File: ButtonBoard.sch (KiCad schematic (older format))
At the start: 4 parts, among them J1 Conn_01x06_Male

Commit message: rearrange and plot for build
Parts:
- D1: footprint LED_THT:LED_D3.0mm -> LEDs:LED_Rectangular_W3.0mm_H2.0mm
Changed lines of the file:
@@
 F 0 "D1" H 6443 2866 50  0000 C CNN
 F 1 "LED" H 6443 2775 50  0000 C CNN
-F 2 "LED_THT:LED_D3.0mm" H 6450 2650 50  0001 C CNN
+F 2 "LEDs:LED_Rectangular_W3.0mm_H2.0mm" H 6450 2650 50  0001 C CNN
 F 3 "~" H 6450 2650 50  0001 C CNN
 	1    6450 2650

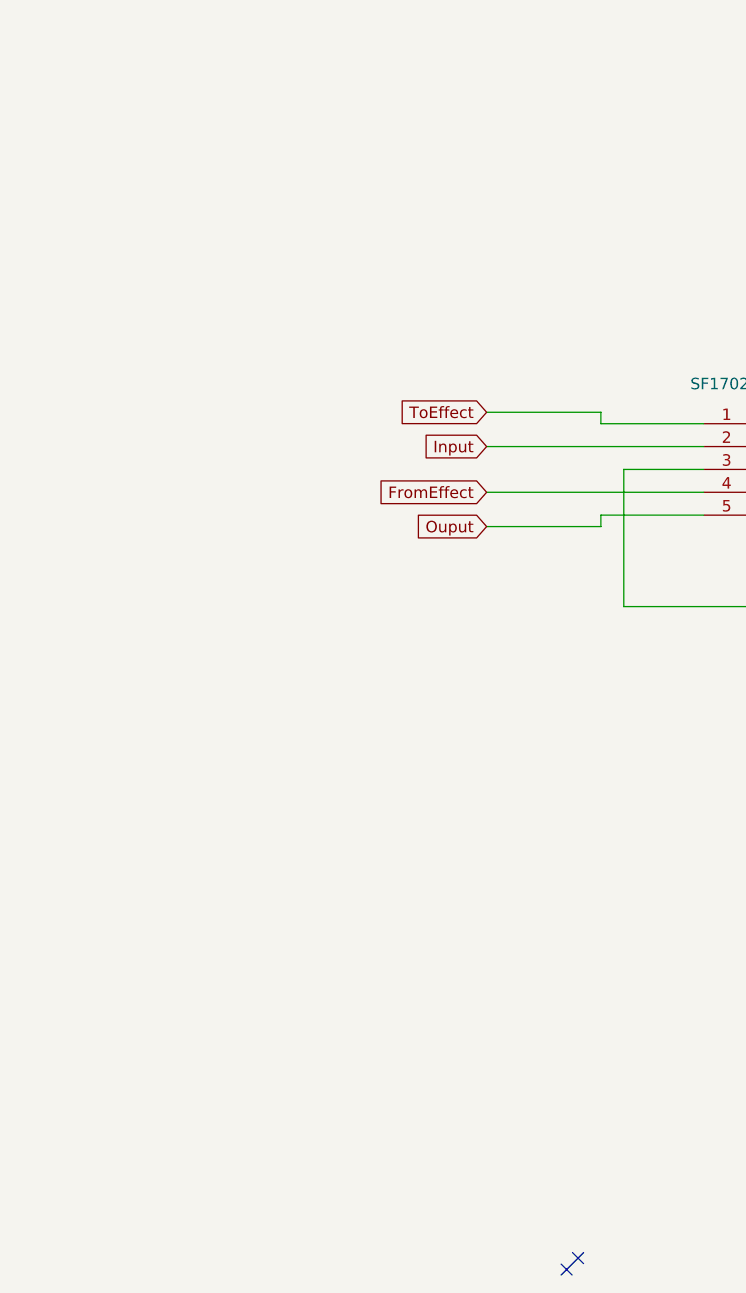
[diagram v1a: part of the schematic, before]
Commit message: Bump to version 1.2 make the holes a little bigger
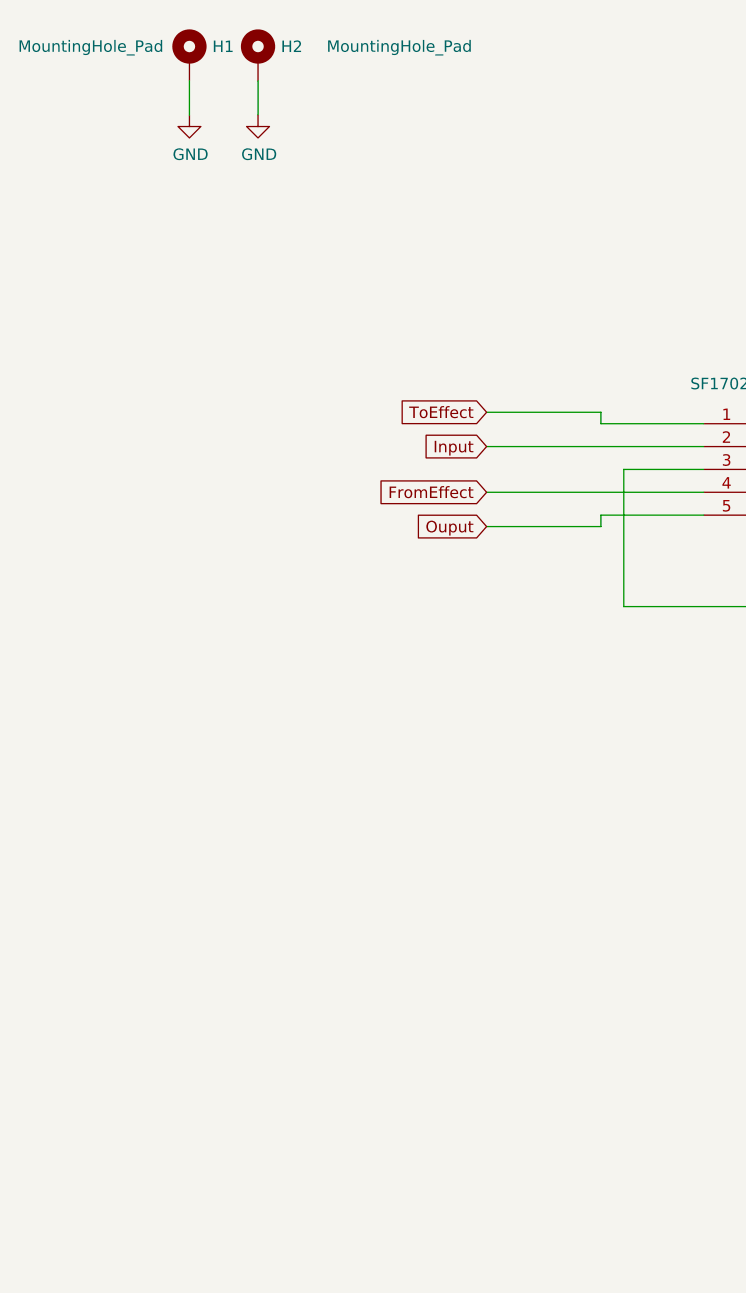
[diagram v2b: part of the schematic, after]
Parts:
- added H1, H2: MountingHole_Pad, Wire_Pads:SolderWirePad_single_1mmDrill, symbol Mechanical:MountingHole_Pad
- S1: footprint SF17020F-0302-21R-L-015:SF17020F030221RL015 -> Footswitch:Footswitch_3PDT
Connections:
- net GND: now also H1.1, H2.1
- no-connect marks 3 -> 1
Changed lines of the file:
@@
 F 0 "S1" H 4850 2915 50  0000 C CNN
 F 1 "SF17020F-0302-21R-L-015" H 4850 2824 50  0000 C CNN
-F 2 "SF17020F-0302-21R-L-015:SF17020F030221RL015" H 5100 2750 50  0001 L CNN
+F 2 "Footswitch:Footswitch_3PDT" H 5100 2750 50  0001 L CNN
 F 3 "https://componentsearchengine.com/Datasheets/1/SF17020F-0302-21R-L-015.pdf" H 5100 2650 50  0001 L CNN
 F 4 "Pushbutton Switches 3PDT STOMP/FOOT SW LATCHING 1A9VDC 9PIN" H 5100 2550 50  0001 L CNN "Description"
@@
 	8350 3250 8150 3250
 Connection ~ 6150 2850
-NoConn ~ 3850 6350
-NoConn ~ 3900 6300
 $Comp
 L Connector:Conn_01x06_Male J1
@@
 Wire Wire Line
 	6500 3450 8350 3450
+$Comp
+L Mechanical:MountingHole_Pad H2
+U 1 1 5CF5505F
+P 2500 1050
+F 0 "H2" H 2600 1099 50  0000 L CNN
+F 1 "MountingHole_Pad" H 2800 1100 50  0000 L CNN
+F 2 "Wire_Pads:SolderWirePad_single_1mmDrill" H 2500 1050 50  0001 C CNN
+F 3 "~" H 2500 1050 50  0001 C CNN
+	1    2500 1050
+	1    0    0    -1
+$EndComp
+$Comp
+L Mechanical:MountingHole_Pad H1
+U 1 1 5CF555B7
+P 2200 1050
+F 0 "H1" H 2300 1099 50  0000 L CNN
+F 1 "MountingHole_Pad" H 1450 1100 50  0000 L CNN
+F 2 "Wire_Pads:SolderWirePad_single_1mmDrill" H 2200 1050 50  0001 C CNN
+F 3 "~" H 2200 1050 50  0001 C CNN
+	1    2200 1050
+	1    0    0    -1
+$EndComp
+$Comp
+L power:GND #PWR0101
+U 1 1 5CF566E5
+P 2200 1300
+F 0 "#PWR0101" H 2200 1050 50  0001 C CNN
+F 1 "GND" H 2205 1127 50  0000 C CNN
+F 2 "" H 2200 1300 50  0001 C CNN
+F 3 "" H 2200 1300 50  0001 C CNN
+	1    2200 1300
+	1    0    0    -1
+$EndComp
+$Comp
+L power:GND #PWR0102
+U 1 1 5CF56BC4
+P 2500 1300
+F 0 "#PWR0102" H 2500 1050 50  0001 C CNN
+F 1 "GND" H 2505 1127 50  0000 C CNN
+F 2 "" H 2500 1300 50  0001 C CNN
+F 3 "" H 2500 1300 50  0001 C CNN
+	1    2500 1300
+	1    0    0    -1
+$EndComp
+Wire Wire Line
+	2200 1300 2200 1150
+Wire Wire Line
+	2500 1300 2500 1150
 $EndSCHEMATC

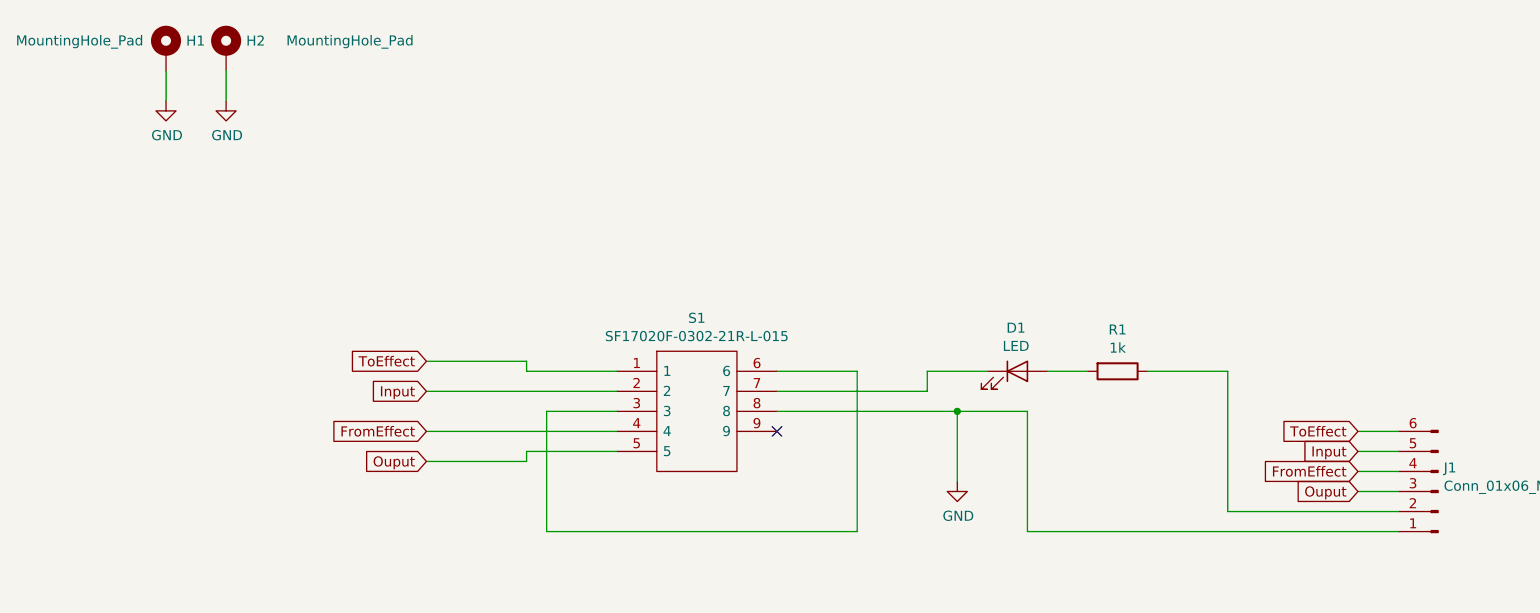
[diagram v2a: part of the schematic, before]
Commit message: re arrange some pins and ground the toEffect pin when bypassed
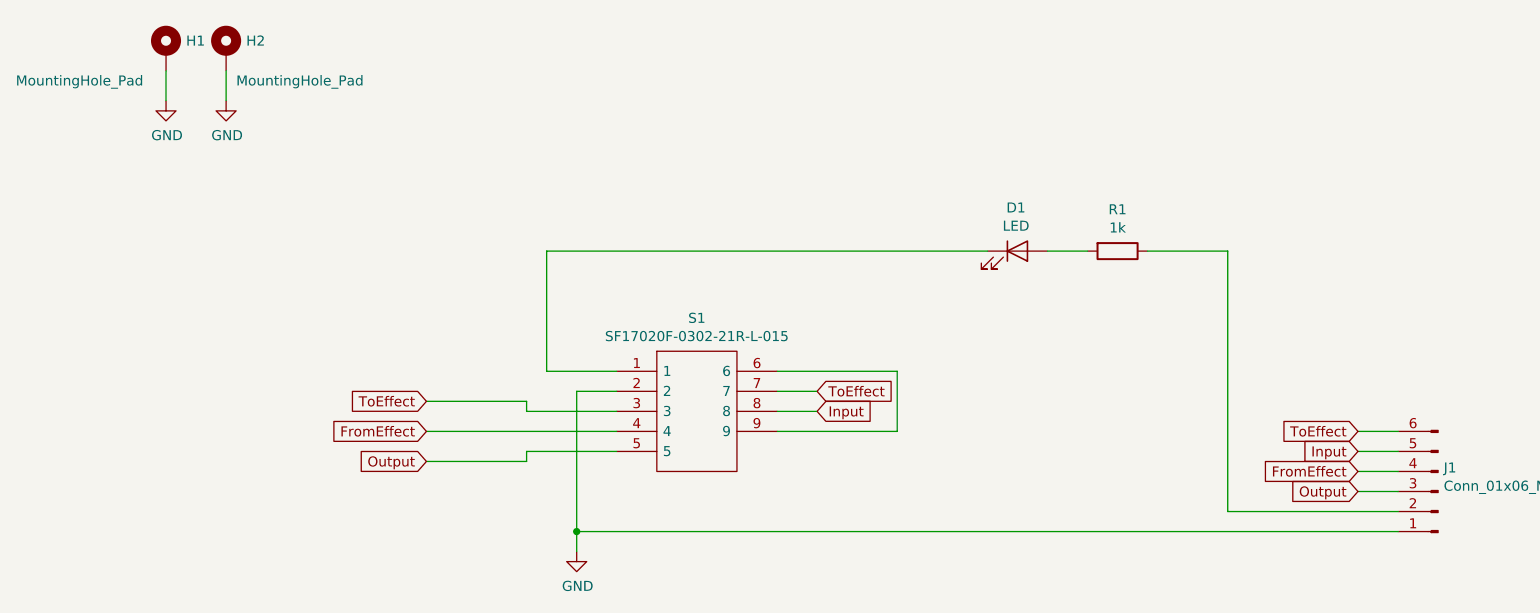
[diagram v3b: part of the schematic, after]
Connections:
- net GND: now also S1.2; no longer S1.8
- net Input: now also S1.8; no longer S1.2
- net ToEffect: now also S1.3, S1.7; no longer S1.1
- net at S1.6: now also S1.9; no longer S1.3
- net at D1.1 (K): now also S1.1; no longer S1.7
- net Ouput renamed Output
- no-connect marks 1 -> 0
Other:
- moved on the sheet: D1, R1
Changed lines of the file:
@@
 L Device:LED D1
 U 1 1 5CDE024C
-P 6450 2650
-F 0 "D1" H 6443 2866 50  0000 C CNN
-F 1 "LED" H 6443 2775 50  0000 C CNN
-F 2 "LEDs:LED_Rectangular_W3.0mm_H2.0mm" H 6450 2650 50  0001 C CNN
-F 3 "~" H 6450 2650 50  0001 C CNN
-	1    6450 2650
+P 6450 2050
+F 0 "D1" H 6443 2266 50  0000 C CNN
+F 1 "LED" H 6443 2175 50  0000 C CNN
+F 2 "LEDs:LED_Rectangular_W3.0mm_H2.0mm" H 6450 2050 50  0001 C CNN
+F 3 "~" H 6450 2050 50  0001 C CNN
+	1    6450 2050
 	1    0    0    -1
 $EndComp
@@
 L Device:R R1
 U 1 1 5CDE095C
-P 6950 2650
-F 0 "R1" V 6743 2650 50  0000 C CNN
-F 1 "1k" V 6834 2650 50  0000 C CNN
-F 2 "Resistor_THT:R_Axial_DIN0204_L3.6mm_D1.6mm_P5.08mm_Horizontal" V 6880 2650 50  0001 C CNN
-F 3 "~" H 6950 2650 50  0001 C CNN
-	1    6950 2650
+P 6950 2050
+F 0 "R1" V 6743 2050 50  0000 C CNN
+F 1 "1k" V 6834 2050 50  0000 C CNN
+F 2 "Resistor_THT:R_Axial_DIN0204_L3.6mm_D1.6mm_P5.08mm_Horizontal" V 6880 2050 50  0001 C CNN
+F 3 "~" H 6950 2050 50  0001 C CNN
+	1    6950 2050
 	0    1    1    0
 $EndComp
-Text GLabel 3500 2750 0    50   Input ~ 0
+Text GLabel 5450 2850 2    50   Input ~ 0
 Input
 Text GLabel 3500 3100 0    50   Input ~ 0
-Ouput
-Text GLabel 3500 2600 0    50   Input ~ 0
+Output
+Text GLabel 5450 2750 2    50   Input ~ 0
 ToEffect
 Text GLabel 3500 2950 0    50   Input ~ 0
 FromEffect
-Wire Wire Line
-	4450 2750 3500 2750
-Wire Wire Line
-	4450 2650 4000 2650
-Wire Wire Line
-	4000 2650 4000 2600
-Wire Wire Line
-	4000 2600 3500 2600
-Wire Wire Line
-	4450 2850 4100 2850
-Wire Wire Line
-	4100 2850 4100 3450
-Wire Wire Line
-	5650 3450 5650 2650
-Wire Wire Line
-	5650 2650 5250 2650
-Wire Wire Line
-	4450 2950 3500 2950
-Wire Wire Line
-	4450 3050 4000 3050
 Wire Wire Line
 	4000 3050 4000 3100
@@
 L power:GND #PWR01
 U 1 1 5CDE8D43
-P 6150 3200
-F 0 "#PWR01" H 6150 2950 50  0001 C CNN
-F 1 "GND" H 6155 3027 50  0000 C CNN
-F 2 "" H 6150 3200 50  0001 C CNN
-F 3 "" H 6150 3200 50  0001 C CNN
-	1    6150 3200
+P 4250 3550
+F 0 "#PWR01" H 4250 3300 50  0001 C CNN
+F 1 "GND" H 4255 3377 50  0000 C CNN
+F 2 "" H 4250 3550 50  0001 C CNN
+F 3 "" H 4250 3550 50  0001 C CNN
+	1    4250 3550
 	1    0    0    -1
 $EndComp
@@
 	9950 1100 9950 1250
 Wire Wire Line
-	6000 2650 6300 2650
+	6600 2050 6800 2050
 Wire Wire Line
-	5250 2750 6000 2750
-Wire Wire Line
-	6000 2750 6000 2650
-Wire Wire Line
-	5250 2850 6150 2850
-Wire Wire Line
-	6150 2850 6150 3200
-Wire Wire Line
-	6600 2650 6800 2650
-Wire Wire Line
-	7100 2650 7500 2650
-NoConn ~ 5250 2950
-Wire Wire Line
-	4100 3450 5650 3450
+	7100 2050 7500 2050
 Text GLabel 8150 2950 0    50   Input ~ 0
 ToEffect
@@
 FromEffect
 Text GLabel 8150 3250 0    50   Input ~ 0
-Ouput
+Output
 Wire Wire Line
 	8150 2950 8350 2950
@@
 Wire Wire Line
 	8350 3250 8150 3250
-Connection ~ 6150 2850
 $Comp
 L Connector:Conn_01x06_Male J1
@@
 $EndComp
 Wire Wire Line
-	6500 2850 6500 3450
-Wire Wire Line
-	6150 2850 6500 2850
-Wire Wire Line
-	7500 2650 7500 3350
+	7500 2050 7500 3350
 Wire Wire Line
 	7500 3350 8350 3350
-Wire Wire Line
-	6500 3450 8350 3450
 $Comp
 L Mechanical:MountingHole_Pad H2
@@
 P 2500 1050
 F 0 "H2" H 2600 1099 50  0000 L CNN
-F 1 "MountingHole_Pad" H 2800 1100 50  0000 L CNN
+F 1 "MountingHole_Pad" H 2550 900 50  0000 L CNN
 F 2 "Wire_Pads:SolderWirePad_single_1mmDrill" H 2500 1050 50  0001 C CNN
 F 3 "~" H 2500 1050 50  0001 C CNN
@@
 P 2200 1050
 F 0 "H1" H 2300 1099 50  0000 L CNN
-F 1 "MountingHole_Pad" H 1450 1100 50  0000 L CNN
+F 1 "MountingHole_Pad" H 1450 900 50  0000 L CNN
 F 2 "Wire_Pads:SolderWirePad_single_1mmDrill" H 2200 1050 50  0001 C CNN
 F 3 "~" H 2200 1050 50  0001 C CNN
@@
 Wire Wire Line
 	2500 1300 2500 1150
+Wire Wire Line
+	4450 2950 3500 2950
+Wire Wire Line
+	4450 2750 4250 2750
+Wire Wire Line
+	4250 2750 4250 3450
+Wire Wire Line
+	4250 3450 8350 3450
+Wire Wire Line
+	4250 3450 4250 3550
+Connection ~ 4250 3450
+Wire Wire Line
+	5450 2850 5250 2850
+Wire Wire Line
+	4450 2650 4100 2650
+Wire Wire Line
+	4100 2650 4100 2050
+Wire Wire Line
+	4000 2850 4450 2850
+Wire Wire Line
+	4000 3050 4450 3050
+Wire Wire Line
+	5250 2650 5850 2650
+Wire Wire Line
+	5850 2650 5850 2950
+Wire Wire Line
+	5850 2950 5250 2950
+Wire Wire Line
+	5250 2750 5450 2750
+Text GLabel 3500 2800 0    50   Input ~ 0
+ToEffect
+Wire Wire Line
+	3500 2800 4000 2800
+Wire Wire Line
+	4000 2800 4000 2850
+Wire Wire Line
+	4100 2050 6300 2050
 $EndSCHEMATC

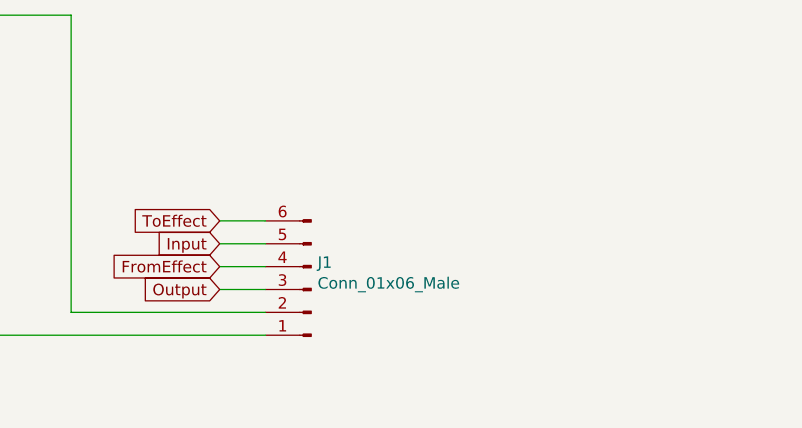
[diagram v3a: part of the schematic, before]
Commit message: update board with better connector
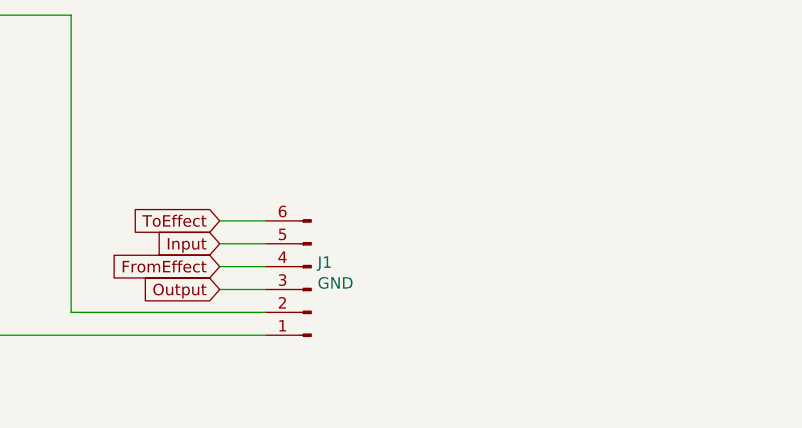
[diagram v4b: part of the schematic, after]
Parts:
- J1: value Conn_01x06_Male -> GND; footprint Connector_PinHeader_2.00mm:PinHeader_1x06_P2.00mm_Vertical -> Connector_PinHeader_2.54mm:PinHeader_1x06_P2.54mm_Vertical
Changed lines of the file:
@@
 P 8550 3250
 F 0 "J1" H 8522 3132 50  0000 R CNN
-F 1 "Conn_01x06_Male" H 8522 3223 50  0000 R CNN
-F 2 "Connector_PinHeader_2.00mm:PinHeader_1x06_P2.00mm_Vertical" H 8550 3250 50  0001 C CNN
+F 1 "GND" H 8522 3223 50  0000 R CNN
+F 2 "Connector_PinHeader_2.54mm:PinHeader_1x06_P2.54mm_Vertical" H 8550 3250 50  0001 C CNN
 F 3 "~" H 8550 3250 50  0001 C CNN
 	1    8550 3250
